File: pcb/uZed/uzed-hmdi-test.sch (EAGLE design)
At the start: 20 parts, among them J5 HDMI-TYPE-A-RECEPTICALFCI1002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, J6 HDMI-TYPE-A-RECEPTICALFCI1002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

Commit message: more work on hdmi -test
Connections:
- net N$11 renamed HDMI_PU
- new net N$13: JX2.P$36
- new net N$17: JX2.P$38
- new net N$6: JX2.P$24
- new net N$7: JX2.P$26
- new net N$8: JX2.P$30
- new net N$9: JX2.P$32
- net P2_CLOCK+: now also JX2.P$18
- net P2_CLOCK-: now also JX2.P$20
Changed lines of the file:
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@@
 <?xml version="1.0" encoding="utf-8"?>
 <!DOCTYPE eagle SYSTEM "eagle.dtd">
-<eagle version="8.6.1">
+<eagle version="8.7.0">
 <drawing>
 <settings>
@@
 </segment>
 </net>
+<net name="P2_CLOCK-" class="0">
+<segment>
+<pinref part="JX2" gate="G$1" pin="P$20"/>
+<wire x1="134.62" y1="132.08" x2="102.87" y2="132.08" width="0.1524" layer="91"/>
+<label x="102.87" y="132.08" size="1.778" layer="95"/>
+</segment>
+</net>
+<net name="N$6" class="0">
+<segment>
+<pinref part="JX2" gate="G$1" pin="P$24"/>
+<wire x1="134.62" y1="127" x2="102.87" y2="127" width="0.1524" layer="91"/>
+</segment>
+</net>
+<net name="N$7" class="0">
+<segment>
+<pinref part="JX2" gate="G$1" pin="P$26"/>
+<wire x1="134.62" y1="124.46" x2="102.87" y2="124.46" width="0.1524" layer="91"/>
+</segment>
+</net>
+<net name="N$8" class="0">
+<segment>
+<pinref part="JX2" gate="G$1" pin="P$30"/>
+<wire x1="134.62" y1="119.38" x2="102.87" y2="119.38" width="0.1524" layer="91"/>
+</segment>
+</net>
+<net name="N$9" class="0">
+<segment>
+<pinref part="JX2" gate="G$1" pin="P$32"/>
+<wire x1="134.62" y1="116.84" x2="102.87" y2="116.84" width="0.1524" layer="91"/>
+</segment>
+</net>
+<net name="N$13" class="0">
+<segment>
+<pinref part="JX2" gate="G$1" pin="P$36"/>
+<wire x1="134.62" y1="111.76" x2="102.87" y2="111.76" width="0.1524" layer="91"/>
+</segment>
+</net>
+<net name="N$17" class="0">
+<segment>
+<pinref part="JX2" gate="G$1" pin="P$38"/>
+<wire x1="134.62" y1="109.22" x2="102.87" y2="109.22" width="0.1524" layer="91"/>
+</segment>
+</net>
+<net name="P2_CLOCK+" class="0">
+<segment>
+<pinref part="JX2" gate="G$1" pin="P$18"/>
+<wire x1="134.62" y1="134.62" x2="102.87" y2="134.62" width="0.1524" layer="91"/>
+<label x="102.87" y="134.62" size="1.778" layer="95"/>
+</segment>
+</net>
 </nets>
 </sheet>
@@
 </segment>
 </net>
-<net name="N$11" class="0">
+<net name="HDMI_PU" class="0">
 <segment>
 <pinref part="RN4" gate="B" pin="2"/>
@@
 <wire x1="116.84" y1="175.26" x2="116.84" y2="177.8" width="0.1524" layer="91"/>
 <junction x="55.88" y="177.8"/>
-</segment>
-</net>
+<label x="82.55" y="177.8" size="1.778" layer="95"/>
+</segment>
+</net>

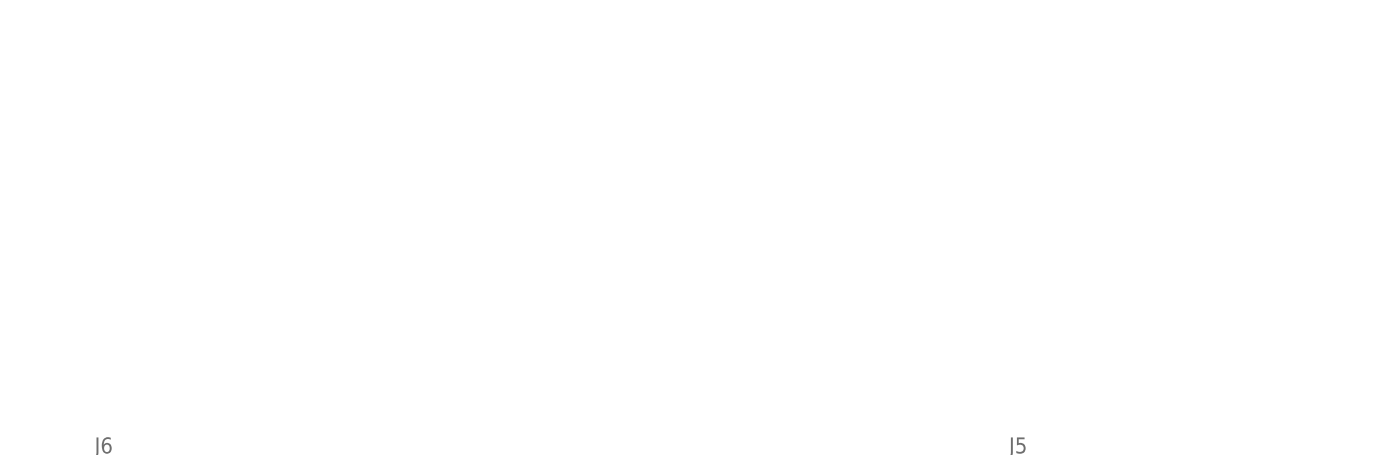
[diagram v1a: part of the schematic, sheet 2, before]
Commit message: finished hdmi test board
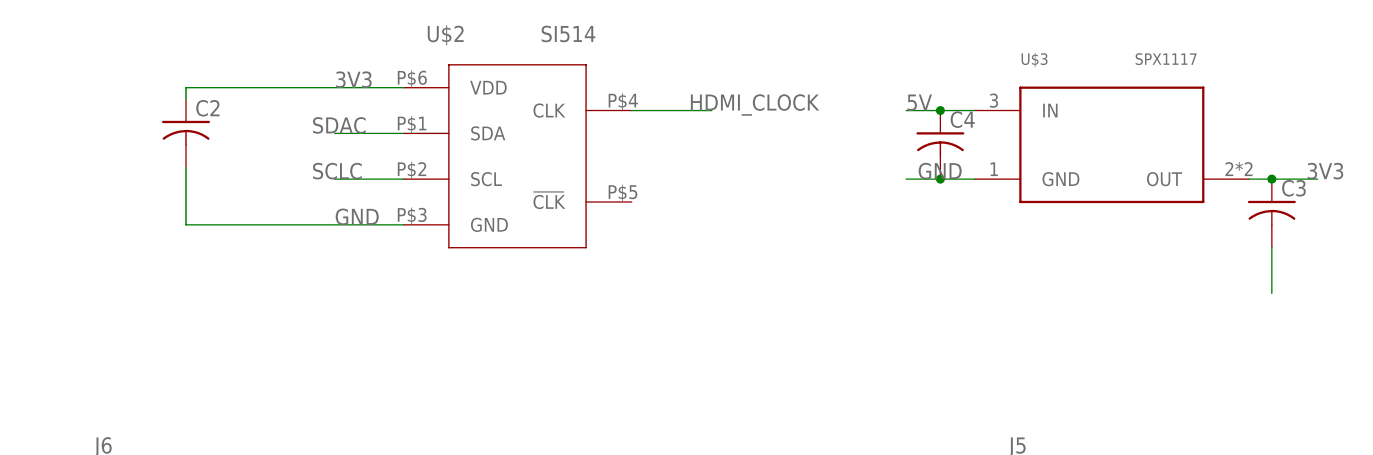
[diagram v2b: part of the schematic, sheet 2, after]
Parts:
- added C2, C3, C4: (no value), rcl:C-USC0603
- added U$2: SI514, lupa300-components:SI514
- added U$3: SPX1117, lupa300-components:SPX1117
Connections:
- removed net N$13: JX2.P$36
- removed net N$17: JX2.P$38
- removed net N$6: JX2.P$24
- removed net N$7: JX2.P$26
- removed net N$8: JX2.P$30
- removed net N$9: JX2.P$32
- new net SCLC: JX2.P$30, U$2.SCL
- new net SDAC: JX2.P$32, U$2.SDA
- net 3V3: now also C2.1, C3.1, U$2.VDD, U$3.OUT
- net 5V: now also C4.1, U$3.IN
- net DET_CONTROL: now also JX2.P$18
- net GND: now also C2.2, C3.2, C4.2, U$2.GND, U$3.GND
- net HDMI_CLOCK: now also JX2.P$48, U$2.CLK; no longer JX1.P$41
- net P2_CLOCK+: now also JX1.P$67; no longer JX2.P$18
- net P2_CLOCK-: now also JX1.P$69; no longer JX2.P$20
- net P2_DATA0+: now also JX1.P$61
- net P2_DATA0-: now also JX1.P$63
- net P2_DATA1+: now also JX1.P$53
- net P2_DATA1-: now also JX1.P$55
- net P2_DATA2+: now also JX1.P$47
- net P2_DATA2-: now also JX1.P$49
- net SCL2: now also JX2.P$24
- net SDA2: now also JX2.P$26
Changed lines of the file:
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@@
 <?xml version="1.0" encoding="utf-8"?>
 <!DOCTYPE eagle SYSTEM "eagle.dtd">
-<eagle version="8.7.0">
+<eagle version="8.6.1">
 <drawing>
 <settings>
@@
 <part name="R6" library="rcl" deviceset="R-US_" device="R0603" value="10K"/>
 <part name="R7" library="rcl" deviceset="R-US_" device="R0603" value="0"/>
+<part name="U$2" library="lupa300-components" deviceset="SI514" device=""/>
+<part name="C2" library="rcl" library_urn="urn:adsk.eagle:library:334" deviceset="C-US" device="C0603" package3d_urn="urn:adsk.eagle:package:23616/2"/>
+<part name="U$3" library="lupa300-components" deviceset="SPX1117" device=""/>
+<part name="C3" library="rcl" library_urn="urn:adsk.eagle:library:334" deviceset="C-US" device="C0603" package3d_urn="urn:adsk.eagle:package:23616/2"/>
+<part name="C4" library="rcl" library_urn="urn:adsk.eagle:library:334" deviceset="C-US" device="C0603" package3d_urn="urn:adsk.eagle:package:23616/2"/>
 </parts>
 <sheets>
@@
 <net name="HDMI_CLOCK" class="0">
 <segment>
-<pinref part="JX1" gate="G$1" pin="P$41"/>
-<wire x1="62.23" y1="105.41" x2="77.47" y2="105.41" width="0.1524" layer="91"/>
-<label x="77.47" y="105.41" size="1.778" layer="95"/>
+<pinref part="JX2" gate="G$1" pin="P$48"/>
+<wire x1="134.62" y1="96.52" x2="104.14" y2="96.52" width="0.1524" layer="91"/>
+<label x="104.14" y="96.52" size="1.778" layer="95"/>
 </segment>
 </net>
@@
 </segment>
 </net>
+<net name="P2_DATA1+" class="0">
+<segment>
+<pinref part="JX1" gate="G$1" pin="P$53"/>
+<wire x1="62.23" y1="90.17" x2="77.47" y2="90.17" width="0.1524" layer="91"/>
+<label x="71.12" y="90.17" size="1.778" layer="95"/>
+</segment>
+</net>
+<net name="P2_DATA1-" class="0">
+<segment>
+<pinref part="JX1" gate="G$1" pin="P$55"/>
+<wire x1="62.23" y1="87.63" x2="77.47" y2="87.63" width="0.1524" layer="91"/>
+<label x="71.12" y="87.63" size="1.778" layer="95"/>
+</segment>
+</net>
+<net name="P2_DATA2+" class="0">
+<segment>
+<pinref part="JX1" gate="G$1" pin="P$47"/>
+<wire x1="62.23" y1="97.79" x2="77.47" y2="97.79" width="0.1524" layer="91"/>
+<label x="78.74" y="97.79" size="1.778" layer="95"/>
+</segment>
+</net>
+<net name="P2_DATA2-" class="0">
+<segment>
+<pinref part="JX1" gate="G$1" pin="P$49"/>
+<wire x1="62.23" y1="95.25" x2="77.47" y2="95.25" width="0.1524" layer="91"/>
+<label x="77.47" y="95.25" size="1.778" layer="95"/>
+</segment>
+</net>
+<net name="P2_DATA0+" class="0">
+<segment>
+<pinref part="JX1" gate="G$1" pin="P$61"/>
+<wire x1="62.23" y1="80.01" x2="77.47" y2="80.01" width="0.1524" layer="91"/>
+<label x="77.47" y="80.01" size="1.778" layer="95"/>
+</segment>
+</net>
+<net name="P2_DATA0-" class="0">
+<segment>
+<pinref part="JX1" gate="G$1" pin="P$63"/>
+<wire x1="62.23" y1="77.47" x2="77.47" y2="77.47" width="0.1524" layer="91"/>
+<label x="77.47" y="77.47" size="1.778" layer="95"/>
+</segment>
+</net>
+<net name="P2_CLOCK+" class="0">
+<segment>
+<pinref part="JX1" gate="G$1" pin="P$67"/>
+<wire x1="62.23" y1="72.39" x2="77.47" y2="72.39" width="0.1524" layer="91"/>
+<label x="77.47" y="72.39" size="1.778" layer="95"/>
+</segment>
+</net>
 <net name="P2_CLOCK-" class="0">
 <segment>
-<pinref part="JX2" gate="G$1" pin="P$20"/>
-<wire x1="134.62" y1="132.08" x2="102.87" y2="132.08" width="0.1524" layer="91"/>
-<label x="102.87" y="132.08" size="1.778" layer="95"/>
-</segment>
-</net>
-<net name="N$6" class="0">
+<pinref part="JX1" gate="G$1" pin="P$69"/>
+<wire x1="62.23" y1="69.85" x2="77.47" y2="69.85" width="0.1524" layer="91"/>
+<label x="77.47" y="69.85" size="1.778" layer="95"/>
+</segment>
+</net>
+<net name="DET_CONTROL" class="0">
+<segment>
+<pinref part="JX2" gate="G$1" pin="P$18"/>
+<wire x1="134.62" y1="134.62" x2="104.14" y2="134.62" width="0.1524" layer="91"/>
+<label x="104.14" y="134.62" size="1.778" layer="95"/>
+</segment>
+</net>
+<net name="SCLC" class="0">
+<segment>
+<pinref part="JX2" gate="G$1" pin="P$30"/>
+<wire x1="134.62" y1="119.38" x2="104.14" y2="119.38" width="0.1524" layer="91"/>
+<label x="104.14" y="119.38" size="1.778" layer="95"/>
+</segment>
+</net>
+<net name="SDAC" class="0">
+<segment>
+<pinref part="JX2" gate="G$1" pin="P$32"/>
+<wire x1="134.62" y1="116.84" x2="104.14" y2="116.84" width="0.1524" layer="91"/>
+<label x="104.14" y="116.84" size="1.778" layer="95"/>
+</segment>
+</net>
+<net name="SCL2" class="0">
 <segment>
 <pinref part="JX2" gate="G$1" pin="P$24"/>
-<wire x1="134.62" y1="127" x2="102.87" y2="127" width="0.1524" layer="91"/>
-</segment>
-</net>
-<net name="N$7" class="0">
+<wire x1="134.62" y1="127" x2="104.14" y2="127" width="0.1524" layer="91"/>
+<label x="104.14" y="127" size="1.778" layer="95"/>
+</segment>
+</net>
+<net name="SDA2" class="0">
 <segment>
 <pinref part="JX2" gate="G$1" pin="P$26"/>
-<wire x1="134.62" y1="124.46" x2="102.87" y2="124.46" width="0.1524" layer="91"/>
-</segment>
-</net>
-<net name="N$8" class="0">
-<segment>
-<pinref part="JX2" gate="G$1" pin="P$30"/>
-<wire x1="134.62" y1="119.38" x2="102.87" y2="119.38" width="0.1524" layer="91"/>
-</segment>
-</net>
-<net name="N$9" class="0">
-<segment>
-<pinref part="JX2" gate="G$1" pin="P$32"/>
-<wire x1="134.62" y1="116.84" x2="102.87" y2="116.84" width="0.1524" layer="91"/>
-</segment>
-</net>
-<net name="N$13" class="0">
-<segment>
-<pinref part="JX2" gate="G$1" pin="P$36"/>
-<wire x1="134.62" y1="111.76" x2="102.87" y2="111.76" width="0.1524" layer="91"/>
-</segment>
-</net>
-<net name="N$17" class="0">
-<segment>
-<pinref part="JX2" gate="G$1" pin="P$38"/>
-<wire x1="134.62" y1="109.22" x2="102.87" y2="109.22" width="0.1524" layer="91"/>
-</segment>
-</net>
-<net name="P2_CLOCK+" class="0">
-<segment>
-<pinref part="JX2" gate="G$1" pin="P$18"/>
-<wire x1="134.62" y1="134.62" x2="102.87" y2="134.62" width="0.1524" layer="91"/>
-<label x="102.87" y="134.62" size="1.778" layer="95"/>
+<wire x1="134.62" y1="124.46" x2="104.14" y2="124.46" width="0.1524" layer="91"/>
 </segment>
 </net>
@@
 <instance part="R6" gate="G$1" x="119.38" y="48.26" rot="R270"/>
 <instance part="R7" gate="G$1" x="218.44" y="74.93" rot="R270"/>
+<instance part="U$2" gate="G$1" x="200.66" y="190.5"/>
+<instance part="C2" gate="G$1" x="163.83" y="194.31"/>
+<instance part="U$3" gate="G$1" x="266.7" y="193.04"/>
+<instance part="C3" gate="G$1" x="284.48" y="185.42"/>
+<instance part="C4" gate="G$1" x="247.65" y="193.04"/>
 </instances>
 <busses>
@@
 <wire x1="45.72" y1="55.88" x2="45.72" y2="26.67" width="0.1524" layer="91"/>
 <pinref part="GND4" gate="1" pin="GND"/>
+</segment>
+<segment>
+<pinref part="U$2" gate="G$1" pin="GND"/>
+<label x="180.34" y="182.88" size="1.778" layer="95"/>
+<pinref part="C2" gate="G$1" pin="2"/>
+<wire x1="163.83" y1="189.23" x2="163.83" y2="182.88" width="0.1524" layer="91"/>
+<wire x1="163.83" y1="182.88" x2="187.96" y2="182.88" width="0.1524" layer="91"/>
+</segment>
+<segment>
+<pinref part="U$3" gate="G$1" pin="GND"/>
+<wire x1="251.46" y1="187.96" x2="247.65" y2="187.96" width="0.1524" layer="91"/>
+<label x="245.11" y="187.96" size="1.778" layer="95"/>
+<pinref part="C4" gate="G$1" pin="2"/>
+<wire x1="247.65" y1="187.96" x2="243.84" y2="187.96" width="0.1524" layer="91"/>
+<junction x="247.65" y="187.96"/>
+</segment>
+<segment>
+<pinref part="C3" gate="G$1" pin="2"/>
+<wire x1="284.48" y1="180.34" x2="284.48" y2="175.26" width="0.1524" layer="91"/>
 </segment>
 </net>
@@
 <label x="119.38" y="57.15" size="1.778" layer="95"/>
 </segment>
+<segment>
+<pinref part="U$2" gate="G$1" pin="VDD"/>
+<label x="180.34" y="198.12" size="1.778" layer="95"/>
+<wire x1="187.96" y1="198.12" x2="163.83" y2="198.12" width="0.1524" layer="91"/>
+<pinref part="C2" gate="G$1" pin="1"/>
+<wire x1="163.83" y1="198.12" x2="163.83" y2="196.85" width="0.1524" layer="91"/>
+</segment>
+<segment>
+<pinref part="U$3" gate="G$1" pin="OUT"/>
+<wire x1="281.94" y1="187.96" x2="284.48" y2="187.96" width="0.1524" layer="91"/>
+<label x="288.29" y="187.96" size="1.778" layer="95"/>
+<pinref part="C3" gate="G$1" pin="1"/>
+<wire x1="284.48" y1="187.96" x2="289.56" y2="187.96" width="0.1524" layer="91"/>
+<junction x="284.48" y="187.96"/>
+</segment>
 </net>
 <net name="N$10" class="0">
@@
 <label x="91.44" y="88.9" size="1.778" layer="95"/>
 </segment>
+<segment>
+<pinref part="U$3" gate="G$1" pin="IN"/>
+<wire x1="251.46" y1="195.58" x2="247.65" y2="195.58" width="0.1524" layer="91"/>
+<label x="243.84" y="195.58" size="1.778" layer="95"/>
+<pinref part="C4" gate="G$1" pin="1"/>
+<wire x1="247.65" y1="195.58" x2="243.84" y2="195.58" width="0.1524" layer="91"/>
+<junction x="247.65" y="195.58"/>
+</segment>
+</net>
+<net name="SDAC" class="0">
+<segment>
+<pinref part="U$2" gate="G$1" pin="SDA"/>
+<wire x1="187.96" y1="193.04" x2="180.34" y2="193.04" width="0.1524" layer="91"/>
+<label x="177.8" y="193.04" size="1.778" layer="95"/>
+</segment>
+</net>
+<net name="SCLC" class="0">
+<segment>
+<pinref part="U$2" gate="G$1" pin="SCL"/>
+<wire x1="187.96" y1="187.96" x2="180.34" y2="187.96" width="0.1524" layer="91"/>
+<label x="177.8" y="187.96" size="1.778" layer="95"/>
+</segment>
+</net>
+<net name="HDMI_CLOCK" class="0">
+<segment>
+<pinref part="U$2" gate="G$1" pin="CLK"/>
+<wire x1="213.36" y1="195.58" x2="222.25" y2="195.58" width="0.1524" layer="91"/>
+<label x="219.71" y="195.58" size="1.778" layer="95"/>
+</segment>
 </net>
 </nets>
@@
 packages will not be understood (or retained) with this version.
 </note>
+<note version="8.4" severity="warning">
+Since Version 8.4, EAGLE supports properties for SPICE simulation.
+Probes in schematics and SPICE mapping objects found in parts and library devices
+will not be understood with this version. Update EAGLE to the latest version
+for full support of SPICE simulation.
+</note>
 </compatibility>
